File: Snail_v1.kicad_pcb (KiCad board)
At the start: 2 copper layers, 40.5 x 23 mm, 79 parts, among them J1 PWM_Connector, J2 USB_C_Receptacle_USB2.0_14P, J3 OUT+, J4 OUT-, J5 Conn_ARM_SWD_TagConnect_TC203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, U1 STM32G431K6Tx, U2 TLV61070ADBV, U3 BQ24074RGT, U4 82400102, U5 TPS63031DSK, U6 FUSB303BTMX, U7 BY25Q32ES, U8 PAM8302AAS

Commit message: Added layout
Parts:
- removed J2: USB_C_Receptacle_USB2.0_14P, Connector_USB:USB_C_Receptacle_GCT_USB4105-xx-A_16P_TopMnt_Horizontal
- removed TP6: TestPoint, TestPoint:TestPoint_Pad_D2.5mm
- added C25: 10uF, Capacitor_SMD:C_0805_2012Metric_Pad1.18x1.45mm_HandSolder, F.Cu at (116.5, 121.6)
- added J6: USB_C_Receptacle_USB2.0_16P, Connector_USB:USB_C_Receptacle_GCT_USB4105-xx-A_16P_TopMnt_Horizontal, F.Cu at (50.0, 118.0)
- added R23: 10kR, Resistor_SMD:R_0805_2012Metric_Pad1.20x1.40mm_HandSolder, F.Cu at (79.8, 124.3)
- added R24: 10kR, Resistor_SMD:R_0805_2012Metric_Pad1.20x1.40mm_HandSolder, F.Cu at (120.2, 123.5)
- added R25: 10kR, Resistor_SMD:R_0805_2012Metric_Pad1.20x1.40mm_HandSolder, F.Cu at (120.2, 121.6)
- added R26: 100kR, Resistor_SMD:R_0805_2012Metric_Pad1.20x1.40mm_HandSolder, F.Cu at (120.2, 125.4)
- BT1, C17, R6, R9: moved to B.Cu
- C21: value 1uF -> 10uF
- C22: footprint KiCad:830059539 -> 830059539:830059539
- C6, R7, U3: moved to F.Cu
- J3, J4: footprint Connector_PinSocket_2.54mm:PinSocket_1x01_P2.54mm_Vertical -> Connector_PinHeader_2.54mm:PinHeader_1x01_P2.54mm_Vertical
- TP1, TP2, TP3, TP4, TP5: footprint TestPoint:TestPoint_Pad_D2.5mm -> TestPoint:TestPoint_Pad_D1.0mm
- U2: footprint Package_DFN_QFN:Texas_RWU0007A_VQFN-7_2x2mm_P0.5mm -> TLV61070A:SOT95P280X145-6N
- moved R4 126.8 mm to (124.9, 114.0), turned to -90 degrees
- moved R5 123.7 mm to (122.1, 115.3), turned to 180 degrees
- moved J3 115.8 mm to (137.4, 125.7)
- moved J4 113.0 mm to (137.4, 122.2)
- moved C8 110.2 mm to (128.8, 114.0), turned to -90 degrees
- moved C7 110.2 mm to (126.9, 114.0), turned to -90 degrees
- moved C5 109.9 mm to (125.0, 110.2), turned to 90 degrees
- moved C20 97.7 mm to (125.3, 121.0), turned to 180 degrees
- moved U8 94.2 mm to (125.4, 123.9)
- moved R12 92.6 mm to (128.4, 119.8), turned to -90 degrees
- moved R13 92.4 mm to (130.3, 119.8), turned to -90 degrees
- moved C21 89.3 mm to (116.5, 123.5)
- moved R1 88.6 mm to (133.5, 115.2)
- moved C19 86.8 mm to (114.6, 115.7), turned to 90 degrees
- moved L1 84.2 mm to (121.9, 110.0), turned to 180 degrees
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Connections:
- BT2 pad 11: SPI?_MISO -> UART?_Rx
- BT2 pad 12: SPI?_MISO -> UART?_Tx
- C21 pad 2: Net-(U8-IN+) -> Net-(C21-Pad2)
- R1 pad 1: unconnected-(R1-Pad1) -> DAC
- R11 pad 2: /extFlash/SPI_nCS -> SPI1_nCS
- TP1 pad 1: SPI?_MISO -> UART?_Tx
- TP2 pad 1: SPI?_MISO -> UART?_Rx
- TP3 pad 1: SPI?_MISO -> SPI1_SCK
- TP4 pad 1: SPI?_MISO -> SPI1_MOSI
- TP5 pad 1: SPI?_MISO -> SPI1_MISO
- U1 pad 10: SPI?_MISO -> SPI1_SCK
- U1 pad 11: SPI?_MISO -> SPI1_MISO
- U1 pad 12: SPI?_MISO -> SPI1_MOSI
- U1 pad 13: SPI?_MISO -> SPI1_nCS
- U1 pad 20: unconnected-(U1-PA10-Pad20) -> LED2
- U1 pad 25: SPI?_MISO -> USB_PWR_OUT1
- U1 pad 26: SPI?_MISO -> USB_PWR_OUT2
- U1 pad 27: SPI?_MISO -> unconnected-(U1-PB4-Pad27)
- U1 pad 28: SPI?_MISO -> unconnected-(U1-PB5-Pad28)
- U1 pad 29: SPI?_MISO -> UART?_Rx
- U1 pad 30: SPI?_MISO -> UART?_Tx
- U1 pad 31: unconnected-(U1-PB8-Pad31) -> Net-(U1-PB8)
- U1 pad 5: unconnected-(U1-PA0-Pad5) -> USB_PWR_nINT
- U1 pad 6: unconnected-(U1-PA1-Pad6) -> LED0
- U1 pad 7: SPI?_MISO -> LED1
- U1 pad 8: SPI?_MISO -> SPI1_MOSI
- U1 pad 9: SPI?_MISO -> DAC
- U6 pad 6: /USB_and_Power/USB_PWR_nINT -> USB_PWR_nINT
- U6 pad 7: /USB_and_Power/USB_PWR_OUT1 -> USB_PWR_OUT1
- U6 pad 8: /USB_and_Power/USB_PWR_OUT2 -> USB_PWR_OUT2
- U7 pad 1: /extFlash/SPI_nCS -> SPI1_nCS
- U7 pad 2: SPI?_MISO -> SPI1_MISO
- U7 pad 5: SPI?_MISO -> SPI1_MOSI
- U7 pad 6: SPI?_MISO -> SPI1_SCK
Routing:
- net +5V: track 0.00 -> 110.5 mm, vias 0 -> 1
- net +OUT: track 17.7 -> 124.4 mm, vias 1 -> 6
- net Net-(BT1-+): track 0.00 -> 81.7 mm, vias 0 -> 1
- net DAC: track 0.00 -> 71.4 mm, vias 0 -> 2
- net GND: track 30.9 -> 81.8 mm, vias 6 -> 31
- net USB_PWR_nINT: track 0.00 -> 40.2 mm, vias 0 -> 1
- net nRST: track 0.00 -> 38.4 mm, vias 0 -> 2
- net USB_PWR_OUT2: track 0.00 -> 36.0 mm, vias 0 -> 1
- net USB_PWR_OUT1: track 0.00 -> 33.6 mm, vias 0 -> 1
- net Net-(BT2-AUDIO): track 0.00 -> 24.4 mm
- net LED0: track 0.00 -> 20.9 mm, vias 0 -> 2
- net UART?_Rx: track 0.00 -> 20.8 mm
- net UART?_Tx: track 0.00 -> 19.6 mm
- net SWDIO: track 5.27 -> 24.7 mm
- net LED1: track 0.00 -> 18.7 mm, vias 0 -> 2
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- added copper zone on In2.Cu, net +3V3
- added copper zone on F.Cu, net +OUT
- added copper zone on F.Cu, net /USB_and_Power/VBUS
- added copper zone on In1.Cu, net GND
- added copper zone on F.Cu, net Net-(BT1-+)
- added copper zone on F.Cu, net Net-(U5-EN)
- removed copper zone on B.Cu, net +OUT
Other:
- board size 40.5 x 23 mm -> 91.4 x 22.8 mm
- copper layers 2 -> 4

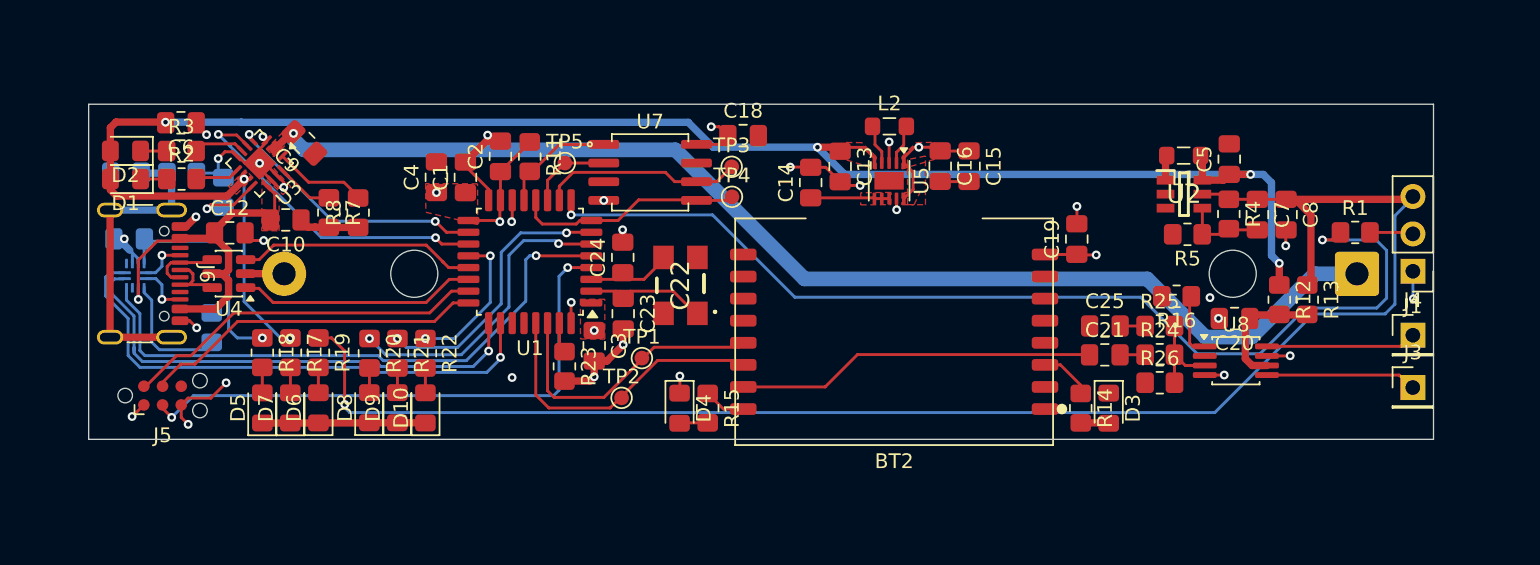
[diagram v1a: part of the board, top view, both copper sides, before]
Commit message: Did Silkscreen + added images of PCBA
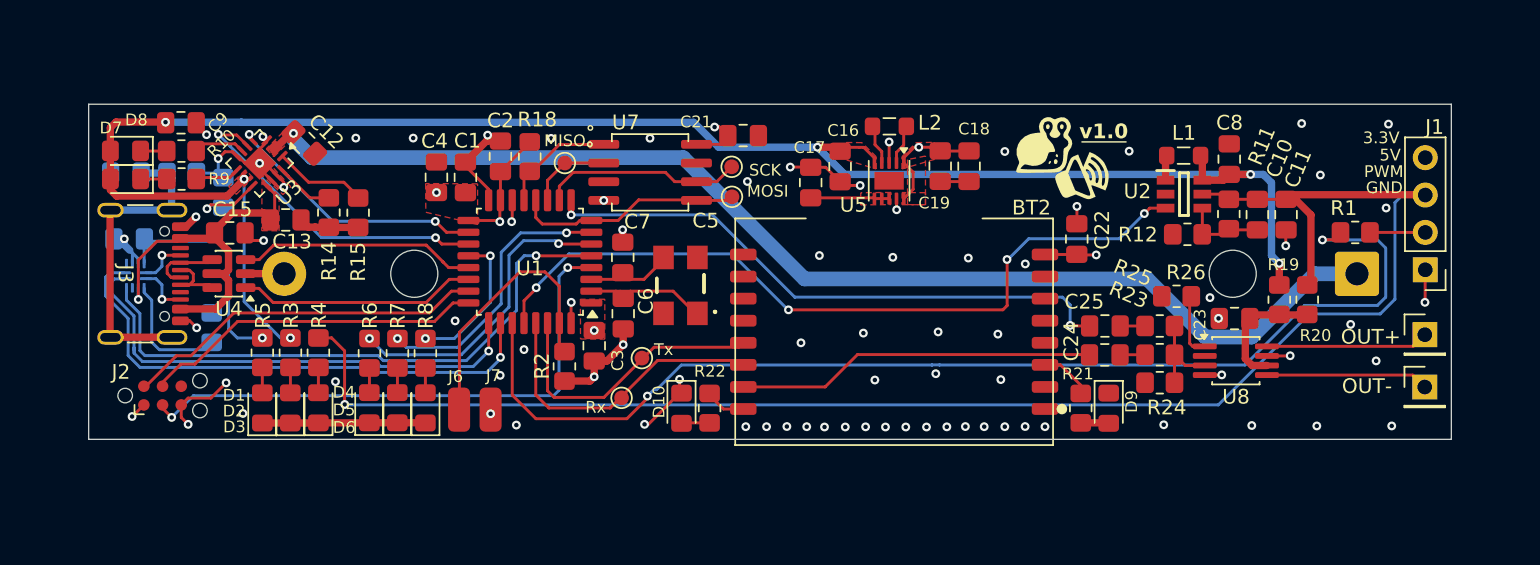
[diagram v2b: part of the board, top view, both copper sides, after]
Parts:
- added G***: LOGO, LOGO, F.Cu at (115.0, 111.5)
- added G***: LOGO, LOGO, F.Cu at (112.3, 109.3)
- added J3: USB_C_Receptacle_USB2.0_16P, Connector_USB:USB_C_Receptacle_GCT_USB4105-xx-A_16P_TopMnt_Horizontal, F.Cu at (50.0, 118.0)
- added J7: Conn_01x01, Connector_Wire:SolderWirePad_1x01_SMD_1.5x3mm, F.Cu at (74.8, 127.2)
- J1: footprint Connector_PinHeader_2.54mm:PinHeader_1x03_P2.54mm_Vertical -> Connector_PinHeader_2.54mm:PinHeader_1x04_P2.54mm_Vertical
- J6: value USB_C_Receptacle_USB2.0_16P -> Conn_01x01; footprint Connector_USB:USB_C_Receptacle_GCT_USB4105-xx-A_16P_TopMnt_Horizontal -> Connector_Wire:SolderWirePad_1x01_SMD_1.5x3mm
- moved J6 24.5 mm to (72.6, 127.2), turned to 0 degrees
- moved J1 0.85 mm to (138.3, 117.7)
- moved J4 0.81 mm to (138.3, 125.7)
- moved J5 0.81 mm to (138.3, 122.2)
- moved D10 0.13 mm to (87.8, 127.1)
- moved R22 0.13 mm to (89.7, 127.1)
- renumbered C7 to C10, C8 to C11, C9 to C12, C10 to C13, C11 to C14, C12 to C15, C13 to C16, C14 to C17, C15 to C18, C16 to C19, C17 to C20, C18 to C21, C19 to C22, C20 to C23, C21 to C24, C22 to C5, C23 to C6, C24 to C7, C5 to C8, C6 to C9, D5 to D1, D4 to D10, D7 to D2, D6 to D3, D8 to D4, D9 to D5, D10 to D6, D1 to D7, D2 to D8, D3 to D9, J5 to J2, J3 to J4, J4 to J5, TP5 to MISO, TP4 to MOSI, R3 to R10, R4 to R11, R5 to R12, R6 to R13, R7 to R14, R8 to R15, R9 to R16, R10 to R17, R11 to R18, R12 to R19, R23 to R2, R13 to R20, R14 to R21, R15 to R22, R24 to R23, R26 to R24, R16 to R26, R17 to R3, R19 to R4, R18 to R5, R20 to R6, R21 to R7, R22 to R8, R2 to R9, TP2 to Rx, TP3 to SCK, TP1 to Tx
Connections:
- net /USB_and_Power/PWR_EN1 renamed PWR_EN1
- net /USB_and_Power/PWR_EN2 renamed PWR_EN2
- net /USB_and_Power/USB+ renamed USB+
- net /USB_and_Power/USB- renamed USB-
- net UART?_Rx renamed UART1_Rx
- net UART?_Tx renamed UART1_Tx
- C20 pad 1: Net-(J6-SHIELD) -> Net-(J3-SHIELD)
- C25 pad 1: /JDY68A/MCU_AUDIO -> MCU_AUDIO
- R1 pad 1: DAC -> PWM
- R16 pad 2: Net-(J6-SHIELD) -> Net-(J3-SHIELD)
- R2 pad 1: Net-(U1-PB8) -> nGPIO0
- U1 pad 27: unconnected-(U1-PB4-Pad27) -> PWM
- U1 pad 28: unconnected-(U1-PB5-Pad28) -> 5V_EN
- U1 pad 31: Net-(U1-PB8) -> nGPIO0
- U1 pad 9: DAC -> MCU_AUDIO
- U2 pad 3: /USB_and_Power/5V_EN -> 5V_EN
- U4 pad 4: Net-(J6-D--PadA7) -> Net-(J3-D--PadA7)
- U4 pad 6: Net-(J6-D+-PadA6) -> Net-(J3-D+-PadA6)
- U6 pad 1: Net-(J6-CC1) -> Net-(J3-CC1)
- U6 pad 2: Net-(J6-CC2) -> Net-(J3-CC2)
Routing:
- net PWM: track 0.00 -> 77.8 mm, vias 0 -> 2
- net DAC: track 71.4 -> 0.00 mm, vias 2 -> 0
- net 5V_EN: track 0.00 -> 52.8 mm, vias 0 -> 4
- net MCU_AUDIO: track 0.00 -> 40.2 mm, vias 0 -> 2
- net Net-(J6-SHIELD): track 21.4 -> 0.00 mm
- net Net-(J3-SHIELD): track 0.00 -> 21.4 mm
- net nGPIO0: track 0.00 -> 18.2 mm
- net Net-(J3-D+-PadA6): track 0.00 -> 5.92 mm
- net Net-(J6-D+-PadA6): track 4.70 -> 0.00 mm
- net Net-(J6-D--PadA7): track 4.70 -> 0.00 mm
- net Net-(J3-D--PadA7): track 0.00 -> 4.70 mm
- net Net-(J6-CC2): track 3.48 -> 0.00 mm, vias 1 -> 0
- net Net-(J3-CC2): track 0.00 -> 3.48 mm, vias 0 -> 1
- net Net-(J6-CC1): track 3.25 -> 0.00 mm, vias 1 -> 0
- net Net-(J3-CC1): track 0.00 -> 3.25 mm, vias 0 -> 1
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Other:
- board size 91.4 x 22.8 mm -> 92.6 x 22.8 mm
- board text added: "18650 li-ion"
- board text added: "3.3V"
- board text added: "5V"
- board text added: "GND"
- board text added: "OUT+"
- board text added: "OUT-"
- board text added: "PWM"
- board text added: "v1.0"

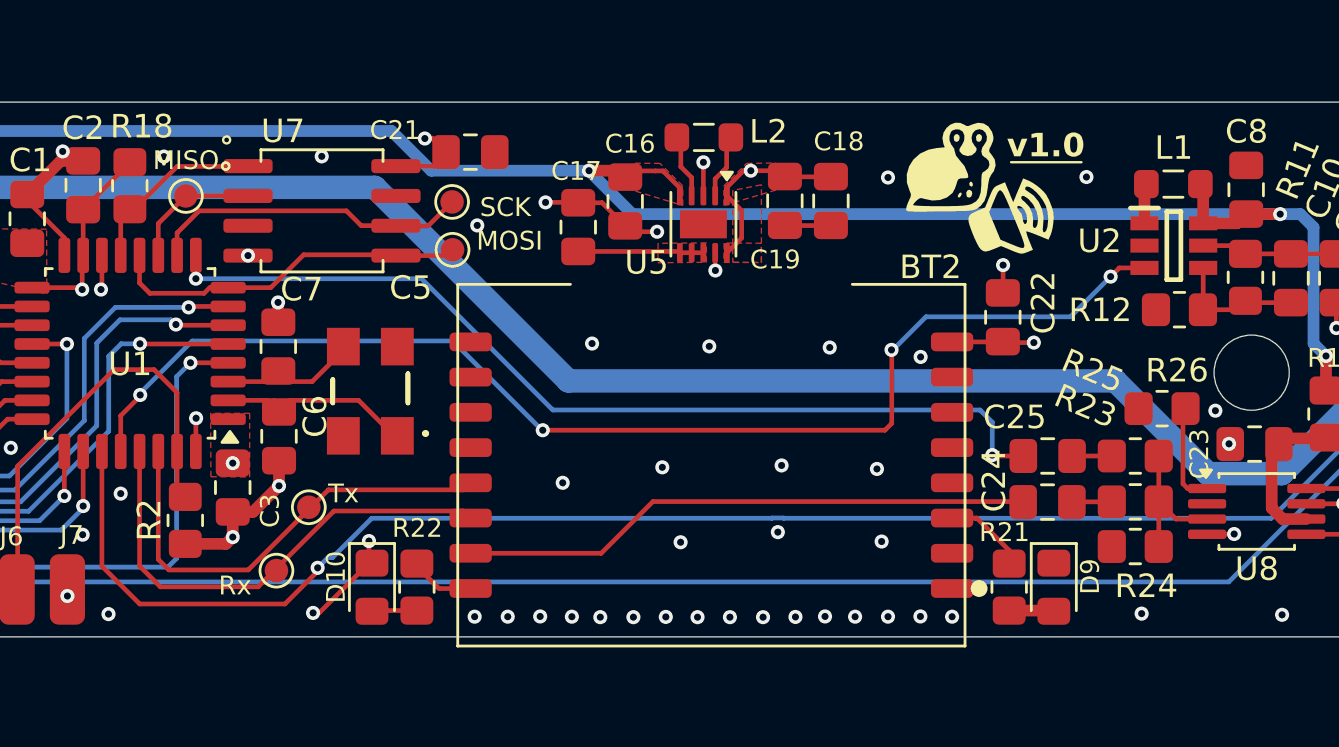
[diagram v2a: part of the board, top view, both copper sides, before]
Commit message: Added missing AMP_nSD connection to MCU via 5V_EN
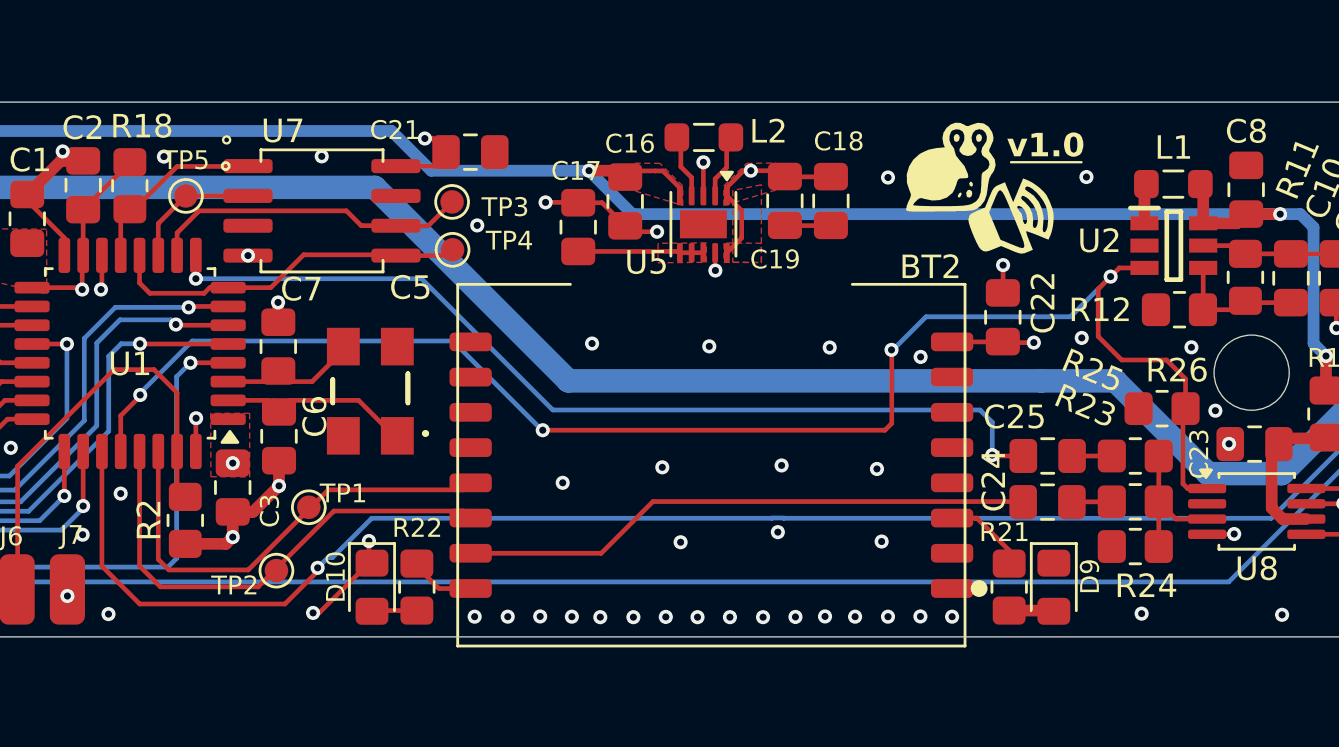
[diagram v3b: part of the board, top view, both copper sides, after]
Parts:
- renumbered Tx to TP1, Rx to TP2, SCK to TP3, MOSI to TP4, MISO to TP5
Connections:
- R26 pad 1: Net-(U8-~{SD}) -> 5V_EN
- U8 pad 1: Net-(U8-~{SD}) -> 5V_EN
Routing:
- net 5V_EN: track 52.8 -> 65.6 mm
- net Net-(U8-~{SD}): track 4.36 -> 0.00 mm
- net GND: vias 81 -> 83
